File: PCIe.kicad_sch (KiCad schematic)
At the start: 24 parts, among them J12 10018783-11200TLF, U15 AP64501SP-13

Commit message: removed HDMI, CAM and DISP1 connectors
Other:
- company: © 2020-2022 Raspberry Pi Ltd (formerly Raspberry Pi (Trading) Ltd.) -> (none)
- title: Compute Module 4 IO Board - PCIe -> Bitcart
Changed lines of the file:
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@@
   (paper "A4")
   (title_block
-    (title "Compute Module 4 IO Board - PCIe")
+    (title "Bitcart")
+    (date "2023-09-15")
     (rev "1")
-    (company "© 2020-2022 Raspberry Pi Ltd (formerly Raspberry Pi (Trading) Ltd.)")
-    (comment 1 "www.raspberrypi.com")
   )
   (junction (at 157.734 152.654) (diameter 1.016) (color 0 0 0 0)

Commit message: extended the board to make room for IO connectors. added the vertical display connector.
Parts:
- TP1: footprint TestPoint:TestPoint_Pad_2.0x2.0mm -> TestPoint:TestPoint_Pad_D1.5mm
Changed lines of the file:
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@@
       (effects (font (size 1.27 1.27)) (justify left))
     )
-    (property "Footprint" "TestPoint:TestPoint_Pad_2.0x2.0mm" (at 242.824 117.094 0)
+    (property "Footprint" "TestPoint:TestPoint_Pad_D1.5mm" (at 242.824 117.094 0)
       (effects (font (size 1.27 1.27)) hide)
     )

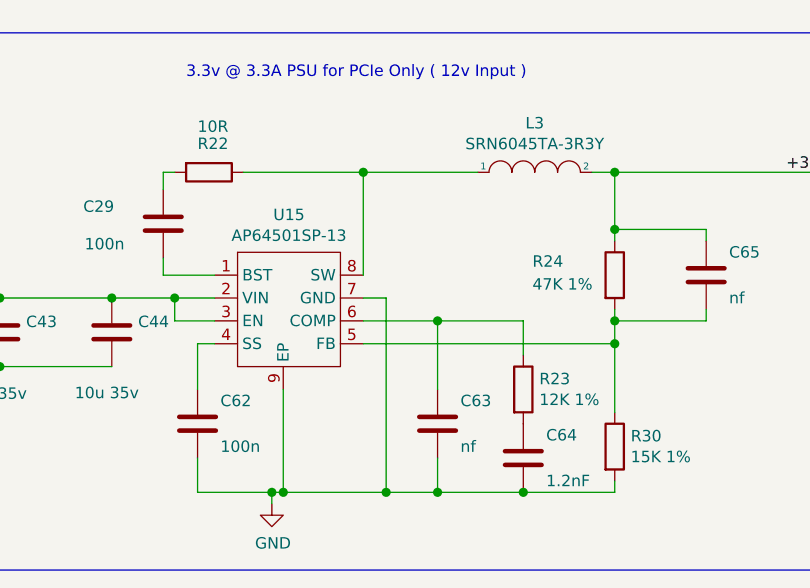
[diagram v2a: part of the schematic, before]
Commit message: added the PSU control connector.
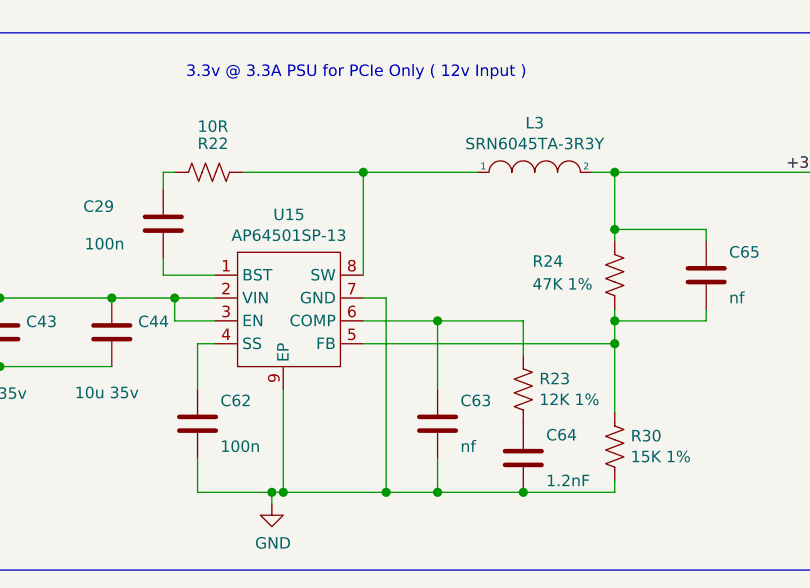
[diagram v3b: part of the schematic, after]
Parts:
- R22, R23, R24, R30: symbol Device:R -> Device:R_US
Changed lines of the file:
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@@
     )
   )
-  (symbol (lib_id "Device:R") (at 183.134 147.574 0) (unit 1)
+  (symbol (lib_id "Device:R_US") (at 183.134 147.574 0) (unit 1)
     (in_bom yes) (on_board yes) (dnp no)
     (property "Reference" "R30" (at 184.912 146.4056 0)
@@
       (effects (font (size 1.27 1.27)) (justify left))
     )
-    (property "Footprint" "Resistor_SMD:R_0402_1005Metric" (at 181.356 147.574 90)
-      (effects (font (size 1.27 1.27)) hide)
-    )
-    (property "Datasheet" "https://fscdn.rohm.com/en/products/databook/datasheet/passive/resistor/chip_resistor/mcr-e.pdf" (at 183.134 147.574 0)
+    (property "Footprint" "Resistor_SMD:R_0402_1005Metric" (at 184.15 147.828 90)
+      (effects (font (size 1.27 1.27)) hide)
+    )
+    (property "Datasheet" "~" (at 183.134 147.574 0)
       (effects (font (size 1.27 1.27)) hide)
     )
@@
     )
   )
-  (symbol (lib_id "Device:R") (at 138.049 117.094 270) (unit 1)
+  (symbol (lib_id "Device:R_US") (at 138.049 117.094 270) (unit 1)
     (in_bom yes) (on_board yes) (dnp no)
     (property "Reference" "R22" (at 136.779 113.919 90)
@@
       (effects (font (size 1.27 1.27)) (justify left))
     )
-    (property "Footprint" "Resistor_SMD:R_0402_1005Metric" (at 138.049 115.316 90)
-      (effects (font (size 1.27 1.27)) hide)
-    )
-    (property "Datasheet" "https://fscdn.rohm.com/en/products/databook/datasheet/passive/resistor/chip_resistor/mcr-e.pdf" (at 138.049 117.094 0)
+    (property "Footprint" "Resistor_SMD:R_0402_1005Metric" (at 137.795 118.11 90)
+      (effects (font (size 1.27 1.27)) hide)
+    )
+    (property "Datasheet" "~" (at 138.049 117.094 0)
       (effects (font (size 1.27 1.27)) hide)
     )
@@
     )
   )
-  (symbol (lib_id "Device:R") (at 172.974 141.224 0) (unit 1)
+  (symbol (lib_id "Device:R_US") (at 172.974 141.224 0) (unit 1)
     (in_bom yes) (on_board yes) (dnp no)
     (property "Reference" "R23" (at 174.752 140.0556 0)
@@
       (effects (font (size 1.27 1.27)) (justify left))
     )
-    (property "Footprint" "Resistor_SMD:R_0402_1005Metric" (at 171.196 141.224 90)
-      (effects (font (size 1.27 1.27)) hide)
-    )
-    (property "Datasheet" "https://fscdn.rohm.com/en/products/databook/datasheet/passive/resistor/chip_resistor/mcr-e.pdf" (at 172.974 141.224 0)
+    (property "Footprint" "Resistor_SMD:R_0402_1005Metric" (at 173.99 141.478 90)
+      (effects (font (size 1.27 1.27)) hide)
+    )
+    (property "Datasheet" "~" (at 172.974 141.224 0)
       (effects (font (size 1.27 1.27)) hide)
     )
@@
     )
   )
-  (symbol (lib_id "Device:R") (at 183.134 128.524 0) (unit 1)
+  (symbol (lib_id "Device:R_US") (at 183.134 128.524 0) (unit 1)
     (in_bom yes) (on_board yes) (dnp no)
     (property "Reference" "R24" (at 173.99 127 0)
@@
       (effects (font (size 1.27 1.27)) (justify left))
     )
-    (property "Footprint" "Resistor_SMD:R_0402_1005Metric" (at 181.356 128.524 90)
-      (effects (font (size 1.27 1.27)) hide)
-    )
-    (property "Datasheet" "https://fscdn.rohm.com/en/products/databook/datasheet/passive/resistor/chip_resistor/mcr-e.pdf" (at 183.134 128.524 0)
-      (effects (font (size 1.27 1.27)) hide)
-    )
+    (property "Footprint" "Resistor_SMD:R_0402_1005Metric" (at 184.15 128.778 90)
+      (effects (font (size 1.27 1.27)) hide)
+    )
+    (property "Datasheet" "~" (at 183.134 128.524 0)
+      (effects (font (size 1.27 1.27)) hide)
+    )

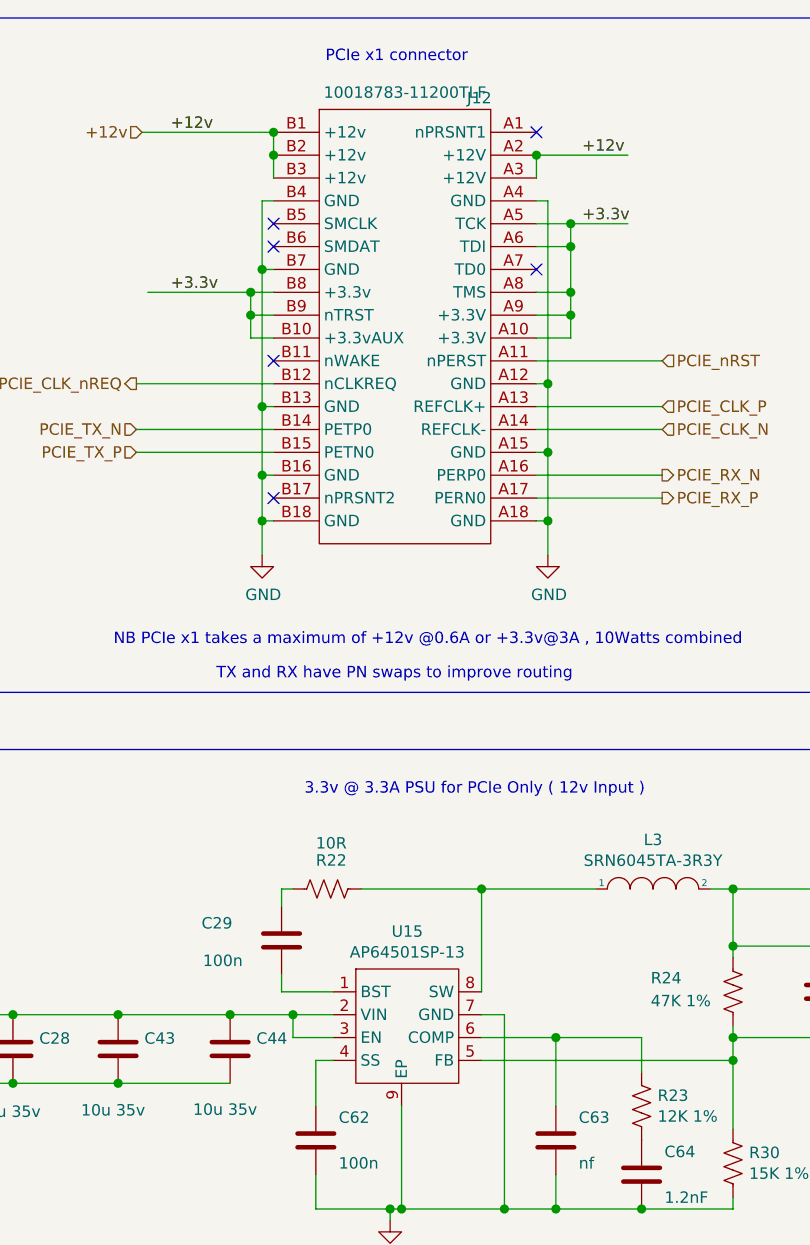
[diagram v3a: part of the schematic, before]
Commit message: finding/adding digikey part numbers
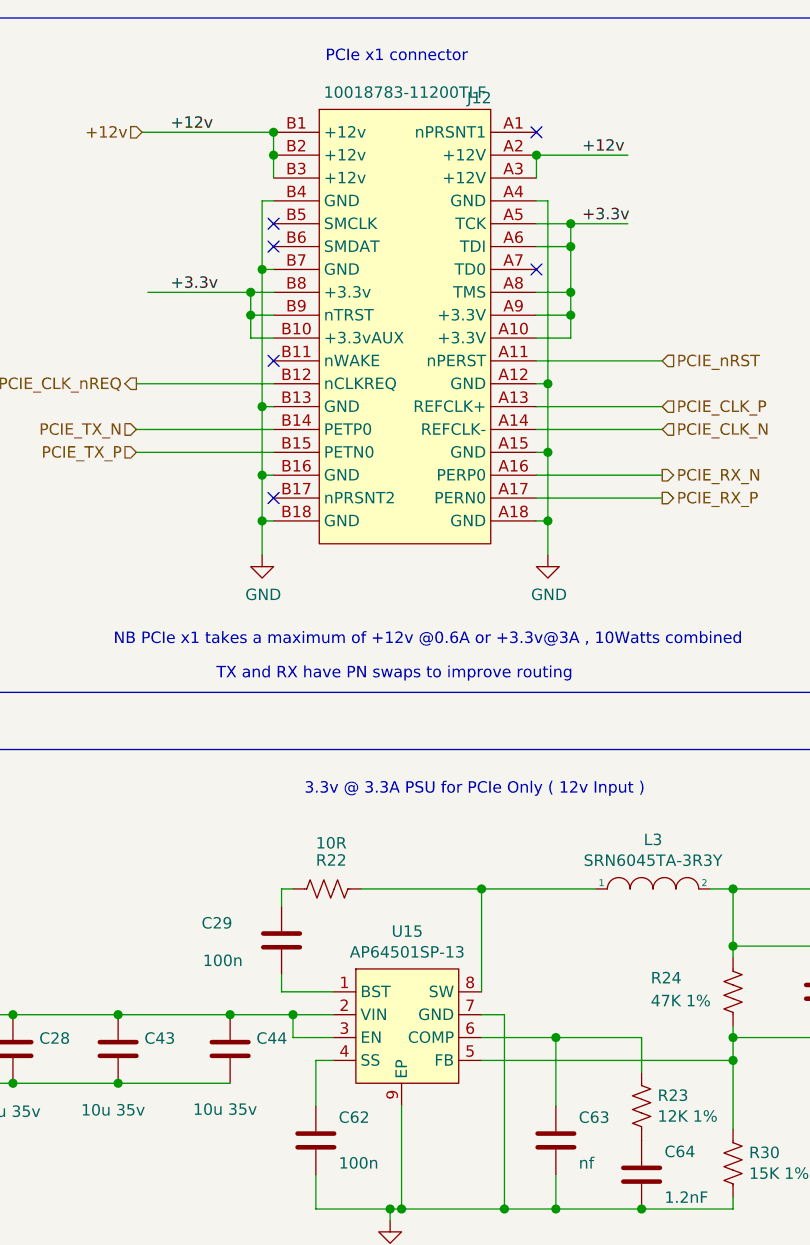
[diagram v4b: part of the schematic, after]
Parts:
- J12: DK (none) -> 609-1998-ND; Field4 Mouser -> (none); Field5 649-10018783-1200TLF -> (none); Field6 10018783-11200TLF -> (none); Field7 Amphenol FCI -> (none); PARTNO (none) -> 10018783-11200TLF; Part Description PCI Express/PCI Connectors PCIE THROUGH HOLE 36P -> (none)
- U15: footprint CM4IO:SOIC-8-1EP_3.9x4.9mm_P1.27mm_EP2.95x4.9mm_Mask2.71x3.4mm_ThermalVias -> Package_SO:SOIC-8-1EP_3.9x4.9mm_P1.27mm_EP2.95x4.9mm_Mask2.71x3.4mm_ThermalVias; DK (none) -> 31-AP64501SP-13CT-ND; Field4 Digikey -> (none); Field5 31-AP64501SP-13CT-ND -> (none); Field6 AP64501SP-13 -> (none); Field7 Diodes -> (none); PARTNO (none) -> AP64501SP-13; Part Description Buck Switching Regulator IC Positive Adjustable 0.8V 1 Outp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 -> (none)
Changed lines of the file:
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@@
       (effects (font (size 1.27 1.27)))
     )
-    (property "Footprint" "CM4IO:SOIC-8-1EP_3.9x4.9mm_P1.27mm_EP2.95x4.9mm_Mask2.71x3.4mm_ThermalVias" (at 146.304 131.064 0)
+    (property "Footprint" "Package_SO:SOIC-8-1EP_3.9x4.9mm_P1.27mm_EP2.95x4.9mm_Mask2.71x3.4mm_ThermalVias" (at 146.304 131.064 0)
       (effects (font (size 1.27 1.27)) hide)
     )
@@
       (effects (font (size 1.27 1.27)) hide)
     )
-    (property "Field4" "Digikey" (at 146.304 131.064 0)
-      (effects (font (size 1.27 1.27)) hide)
-    )
-    (property "Field5" "31-AP64501SP-13CT-ND" (at 146.304 131.064 0)
-      (effects (font (size 1.27 1.27)) hide)
-    )
-    (property "Field6" "AP64501SP-13" (at 146.304 131.064 0)
-      (effects (font (size 1.27 1.27)) hide)
-    )
-    (property "Field7" "Diodes" (at 146.304 131.064 0)
-      (effects (font (size 1.27 1.27)) hide)
-    )
-    (property "Part Description" "Buck Switching Regulator IC Positive Adjustable 0.8V 1 Output 5A 8-SOIC (0.154\", 3.90mm Width) Exposed Pad" (at 146.304 131.064 0)
+    (property "DK" "31-AP64501SP-13CT-ND" (at 146.304 131.064 0)
+      (effects (font (size 1.27 1.27)) hide)
+    )
+    (property "PARTNO" "AP64501SP-13" (at 146.304 131.064 0)
       (effects (font (size 1.27 1.27)) hide)
     )
@@
       (effects (font (size 1.27 1.27)) hide)
     )
-    (property "Field4" "Mouser" (at 151.13 66.04 0)
-      (effects (font (size 1.27 1.27)) hide)
-    )
-    (property "Field5" "649-10018783-1200TLF" (at 151.13 66.04 0)
-      (effects (font (size 1.27 1.27)) hide)
-    )
-    (property "Part Description" "PCI Express/PCI Connectors PCIE THROUGH HOLE 36P" (at 151.13 66.04 0)
-      (effects (font (size 1.27 1.27)) hide)
-    )
-    (property "Field6" "10018783-11200TLF" (at 151.13 66.04 0)
-      (effects (font (size 1.27 1.27)) hide)
-    )
-    (property "Field7" "Amphenol FCI" (at 151.13 66.04 0)
-      (effects (font (size 1.27 1.27)) hide)
-    )
+    (property "DK" "609-1998-ND" (at 151.13 66.04 0)
+      (effects (font (size 1.27 1.27)) hide)
+    )
+    (property "PARTNO" "10018783-11200TLF" (at 151.13 66.04 0)
+      (effects (font (size 1.27 1.27)) hide)
+    )

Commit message: added a lot more parts
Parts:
- C29, C62: value 100n -> 0.1uF; DK (none) -> 478-KGM05AR71C104KHCT-ND; PARTNO (none) -> KGM05AR71C104KH; Part Description 0.1uF 10% 16V Ceramic Capacitor X7R 0402 (1005 Metric) -> (none)
- L3: DK (none) -> SRN6045TA-3R3YCT-ND; Field4 Farnell -> (none); Field5 2616889 -> (none); Field7 Bourns -> (none); Part Description 3.3µH Semi-Shielded Wirewound Inductor 7.8A 21mOhm Nonstand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 -> (none)
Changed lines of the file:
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@@
       (effects (font (size 1.27 1.27)) (justify left))
     )
-    (property "Value" "100n" (at 124.2314 125.0696 0)
+    (property "Value" "0.1uF" (at 124.2314 125.0696 0)
       (effects (font (size 1.27 1.27)) (justify left))
     )
@@
       (effects (font (size 1.27 1.27)) hide)
     )
-    (property "Part Description" "	0.1uF 10% 16V Ceramic Capacitor X7R 0402 (1005 Metric)" (at 132.969 122.809 0)
+    (property "Part Description" "" (at 132.969 122.809 0)
       (effects (font (size 1.27 1.27)) hide)
     )
@@
       (effects (font (size 1.27 1.27)) hide)
     )
+    (property "DK" "478-KGM05AR71C104KHCT-ND" (at 132.969 122.809 0)
+      (effects (font (size 1.27 1.27)) hide)
+    )
+    (property "PARTNO" "KGM05AR71C104KH" (at 132.969 122.809 0)
+      (effects (font (size 1.27 1.27)) hide)
+    )
     (pin "1")
     (pin "2")
@@
       (effects (font (size 1.27 1.27)) (justify left))
     )
-    (property "Value" "100n" (at 139.319 147.574 0)
+    (property "Value" "0.1uF" (at 139.319 147.574 0)
       (effects (font (size 1.27 1.27)) (justify left))
     )
@@
       (effects (font (size 1.27 1.27)) hide)
     )
-    (property "Part Description" "	0.1uF 10% 16V Ceramic Capacitor X7R 0402 (1005 Metric)" (at 136.779 145.034 0)
+    (property "Part Description" "" (at 136.779 145.034 0)
       (effects (font (size 1.27 1.27)) hide)
     )
     (property "Field8" "110091611" (at 136.779 145.034 0)
+      (effects (font (size 1.27 1.27)) hide)
+    )
+    (property "DK" "478-KGM05AR71C104KHCT-ND" (at 136.779 145.034 0)
+      (effects (font (size 1.27 1.27)) hide)
+    )
+    (property "PARTNO" "KGM05AR71C104KH" (at 136.779 145.034 0)
       (effects (font (size 1.27 1.27)) hide)
     )
@@
       (effects (font (size 1.27 1.27)) hide)
     )
-    (property "Field4" "Farnell" (at 174.244 117.094 0)
-      (effects (font (size 1.27 1.27)) hide)
-    )
-    (property "Field5" "2616889" (at 174.244 117.094 0)
+    (property "DK" "SRN6045TA-3R3YCT-ND" (at 174.244 117.094 0)
       (effects (font (size 1.27 1.27)) hide)
     )
@@
       (effects (font (size 1.27 1.27)) hide)
     )
-    (property "Field7" "Bourns" (at 174.244 117.094 0)
-      (effects (font (size 1.27 1.27)) hide)
-    )
-    (property "Part Description" "3.3µH Semi-Shielded Wirewound Inductor 7.8A 21mOhm Nonstandard" (at 174.244 117.094 0)
-      (effects (font (size 1.27 1.27)) hide)
-    )

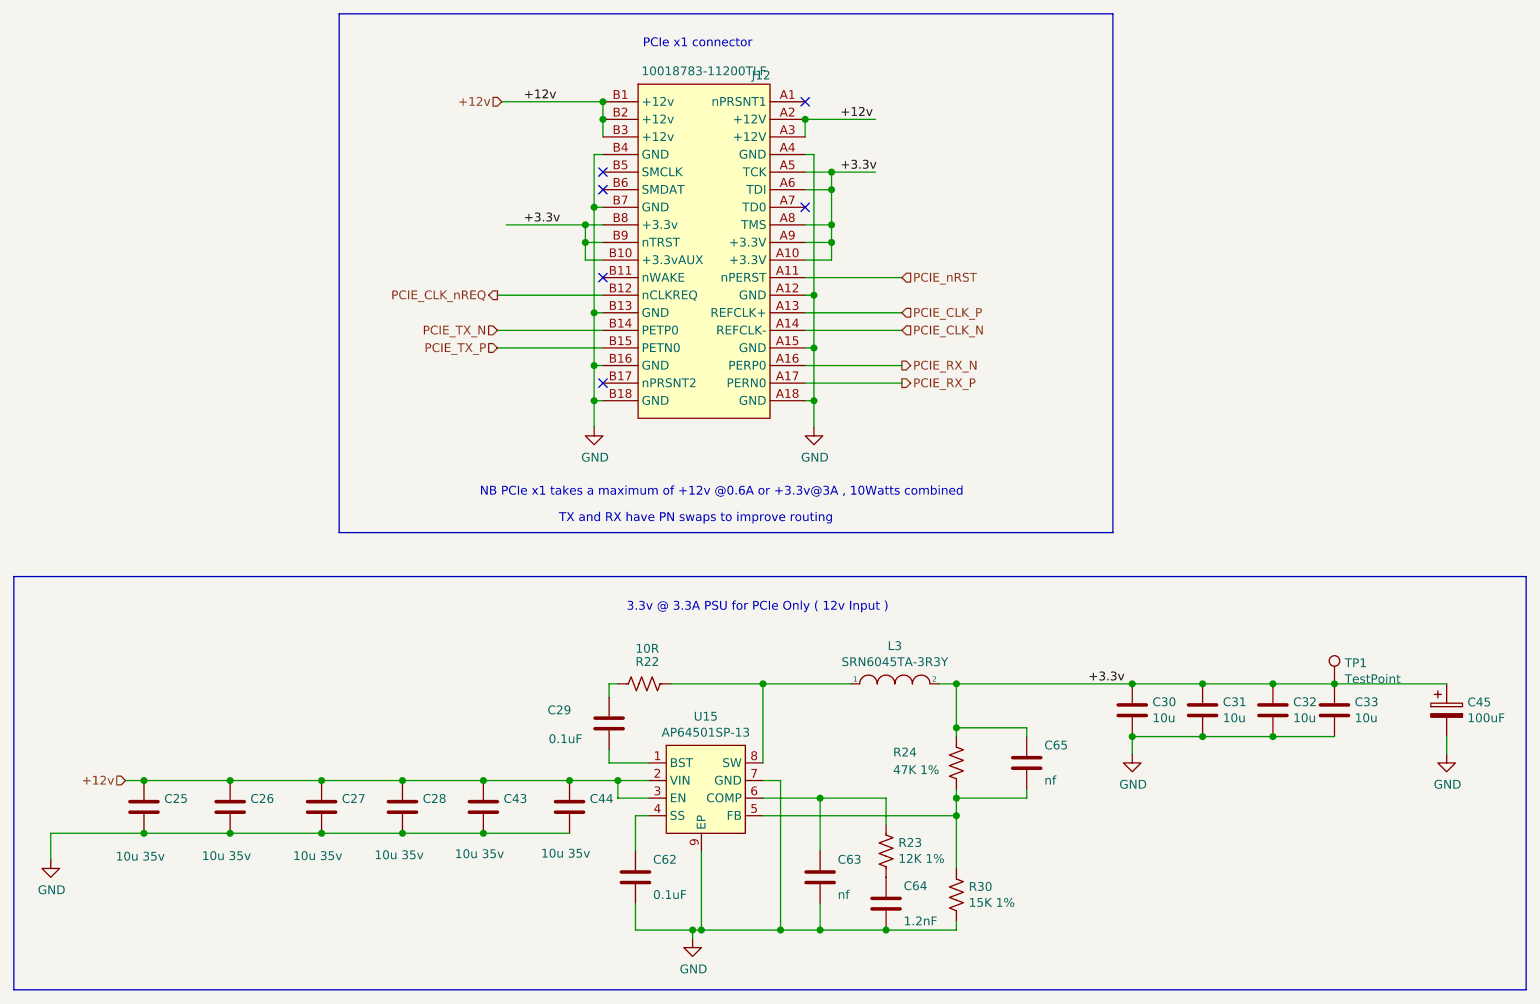
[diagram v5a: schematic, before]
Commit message: resolved some schematic-board errors. switched to tap-on-top ethernet.
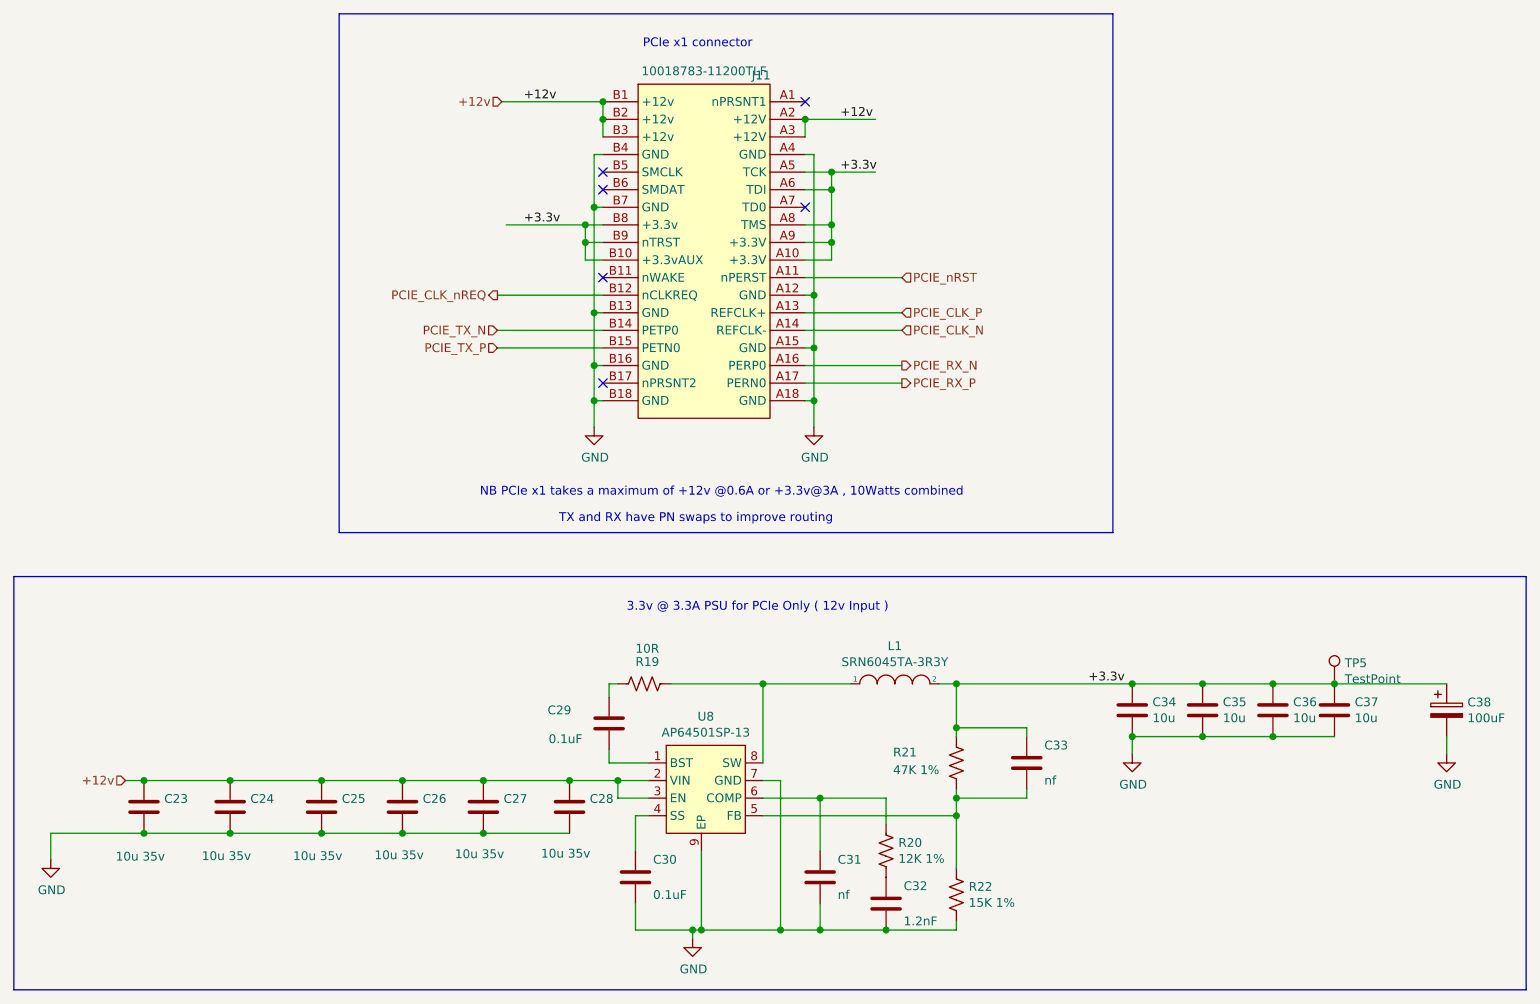
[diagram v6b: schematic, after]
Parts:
- renumbered C25 to C23, C26 to C24, C27 to C25, C28 to C26, C43 to C27, C44 to C28, C62 to C30, C63 to C31, C64 to C32, C65 to C33, C30 to C34, C31 to C35, C32 to C36, C33 to C37, C45 to C38, J12 to J11, L3 to L1, R22 to R19, R23 to R20, R24 to R21, R30 to R22, TP1 to TP5, U15 to U8
